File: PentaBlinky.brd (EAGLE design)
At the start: 40.6 x 22.9 mm, 14 parts, among them J1 AVR_SPI_PRG_6LABELED

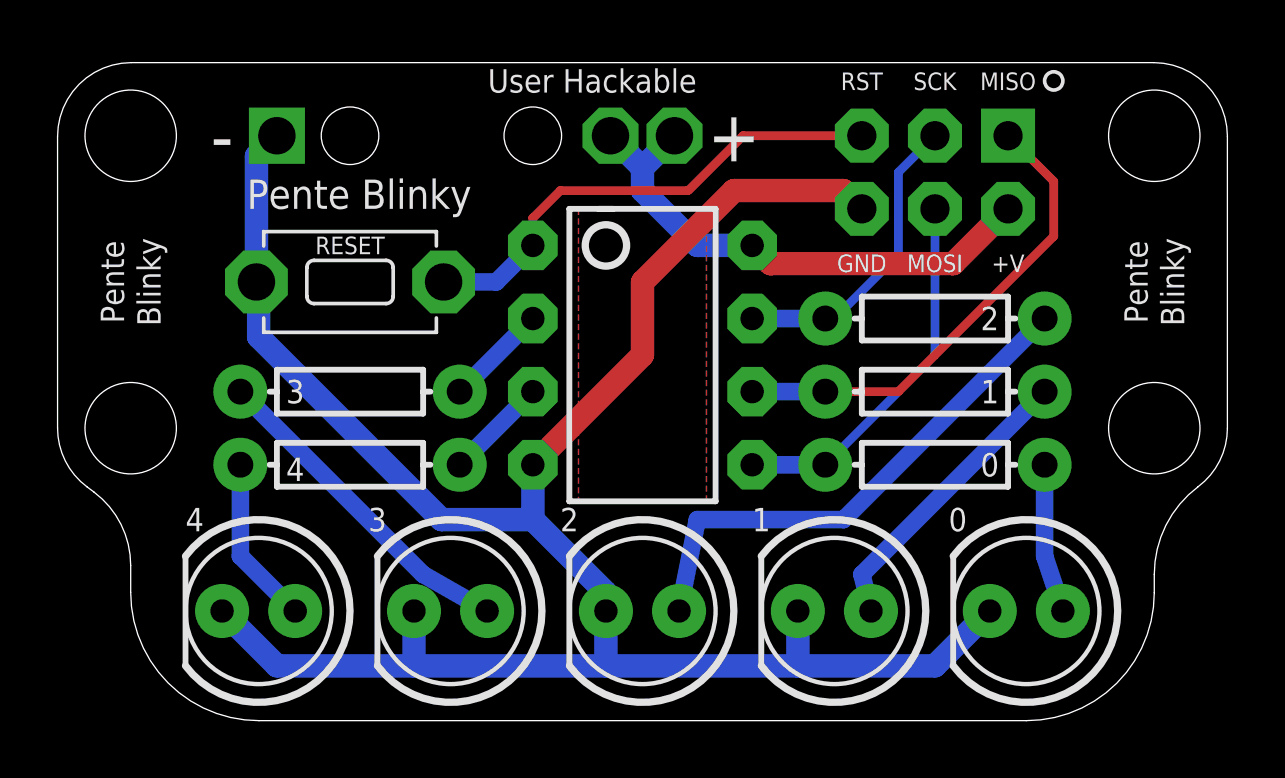
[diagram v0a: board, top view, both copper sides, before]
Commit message: fixing back traces
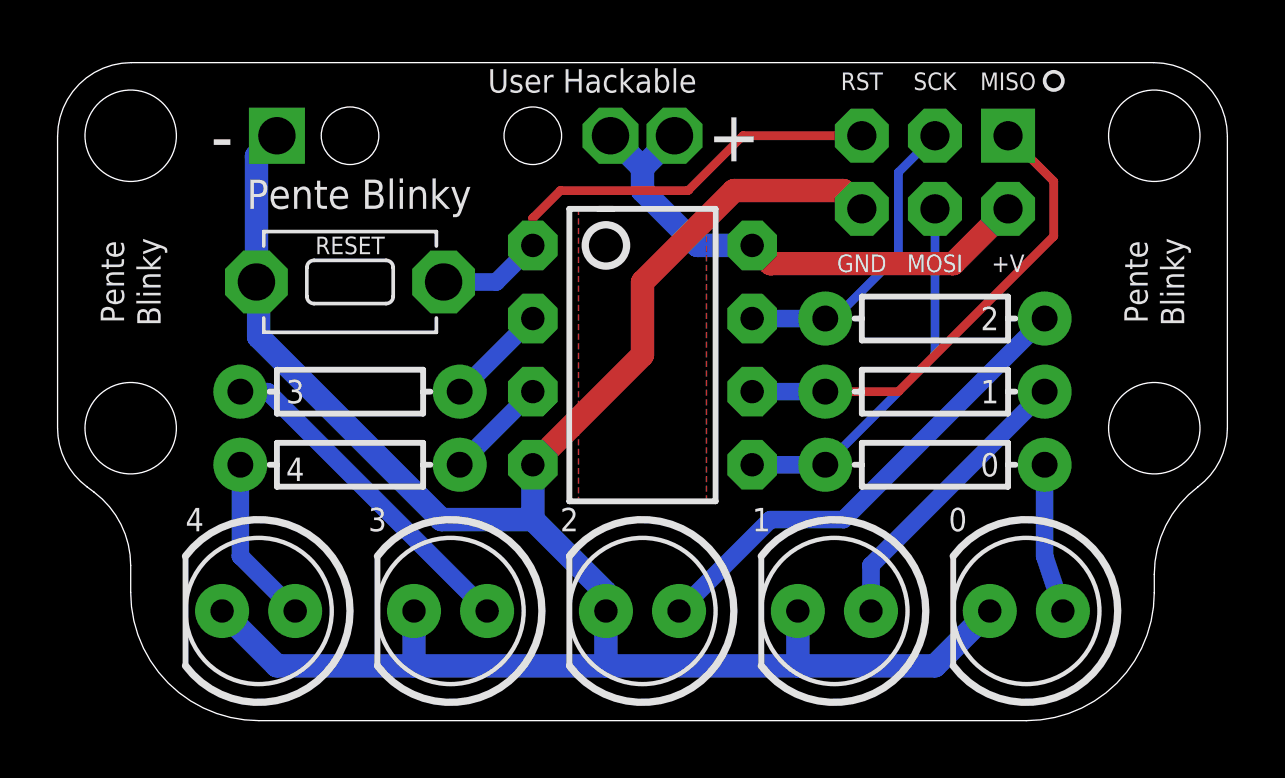
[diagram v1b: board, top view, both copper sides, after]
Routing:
- net N$3: track 18.2 -> 16.9 mm
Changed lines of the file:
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@@
 <contactref element="LED2" pad="A"/>
 <contactref element="R2" pad="P$2"/>
-<wire x1="28.2575" y1="3.81" x2="27.94" y2="5.08" width="0.6096" layer="16"/>
-<wire x1="27.94" y1="5.08" x2="34.29" y2="11.43" width="0.6096" layer="16"/>
+<wire x1="28.2575" y1="3.81" x2="28.2575" y2="5.3975" width="0.6096" layer="16"/>
+<wire x1="28.2575" y1="5.3975" x2="34.29" y2="11.43" width="0.6096" layer="16"/>
 </signal>
 <signal name="N$3">
 <contactref element="LED3" pad="A"/>
 <contactref element="R3" pad="P$2"/>
-<wire x1="21.59" y1="3.81" x2="22.225" y2="6.985" width="0.6096" layer="16"/>
-<wire x1="22.225" y1="6.985" x2="27.305" y2="6.985" width="0.6096" layer="16"/>
+<wire x1="21.59" y1="3.81" x2="24.765" y2="6.985" width="0.6096" layer="16"/>
+<wire x1="24.765" y1="6.985" x2="27.305" y2="6.985" width="0.6096" layer="16"/>
 <wire x1="27.305" y1="6.985" x2="34.29" y2="13.97" width="0.6096" layer="16"/>
 </signal>
@@
 <contactref element="LED4" pad="A"/>
 <contactref element="R4" pad="P$2"/>
-<wire x1="6.35" y1="11.43" x2="12.7" y2="5.08" width="0.6096" layer="16"/>
-<wire x1="12.7" y1="5.08" x2="14.9225" y2="3.81" width="0.6096" layer="16"/>
+<wire x1="6.35" y1="11.43" x2="7.3025" y2="11.43" width="0.6096" layer="16"/>
+<wire x1="7.3025" y1="11.43" x2="14.9225" y2="3.81" width="0.6096" layer="16"/>
 </signal>
 <signal name="N$5">
